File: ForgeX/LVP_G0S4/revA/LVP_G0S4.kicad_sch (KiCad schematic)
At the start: 73 parts, among them J1 Conn_02x05_Odd_Even, J10 Conn_01x02_Pin, J11 Conn_01x02_Pin, J12 Conn_01x02_Pin, J13 Conn_01x02_Pin, J14 Conn_02x05_Odd_Even, J16 Conn_01x04, J17 Conn_01x04, J2 Conn_02x05_Odd_Even, J3 Conn_02x05_Odd_Even, J4 Conn_02x05_Odd_Even, J5 Conn_01x04_Pin, J6 Conn_02x20_Odd_Even, J7 Conn_01x02_Pin, J8 Conn_01x02_Pin, J9 Screw_Terminal_01x09, Q2 AO3400A, U1 SP485EEN-TD, U2 SP485EEN-TD, U3 SP485EEN-TD, U4 AMS1117-3.3, U5 LM311, U6 LM311, U7 LM311

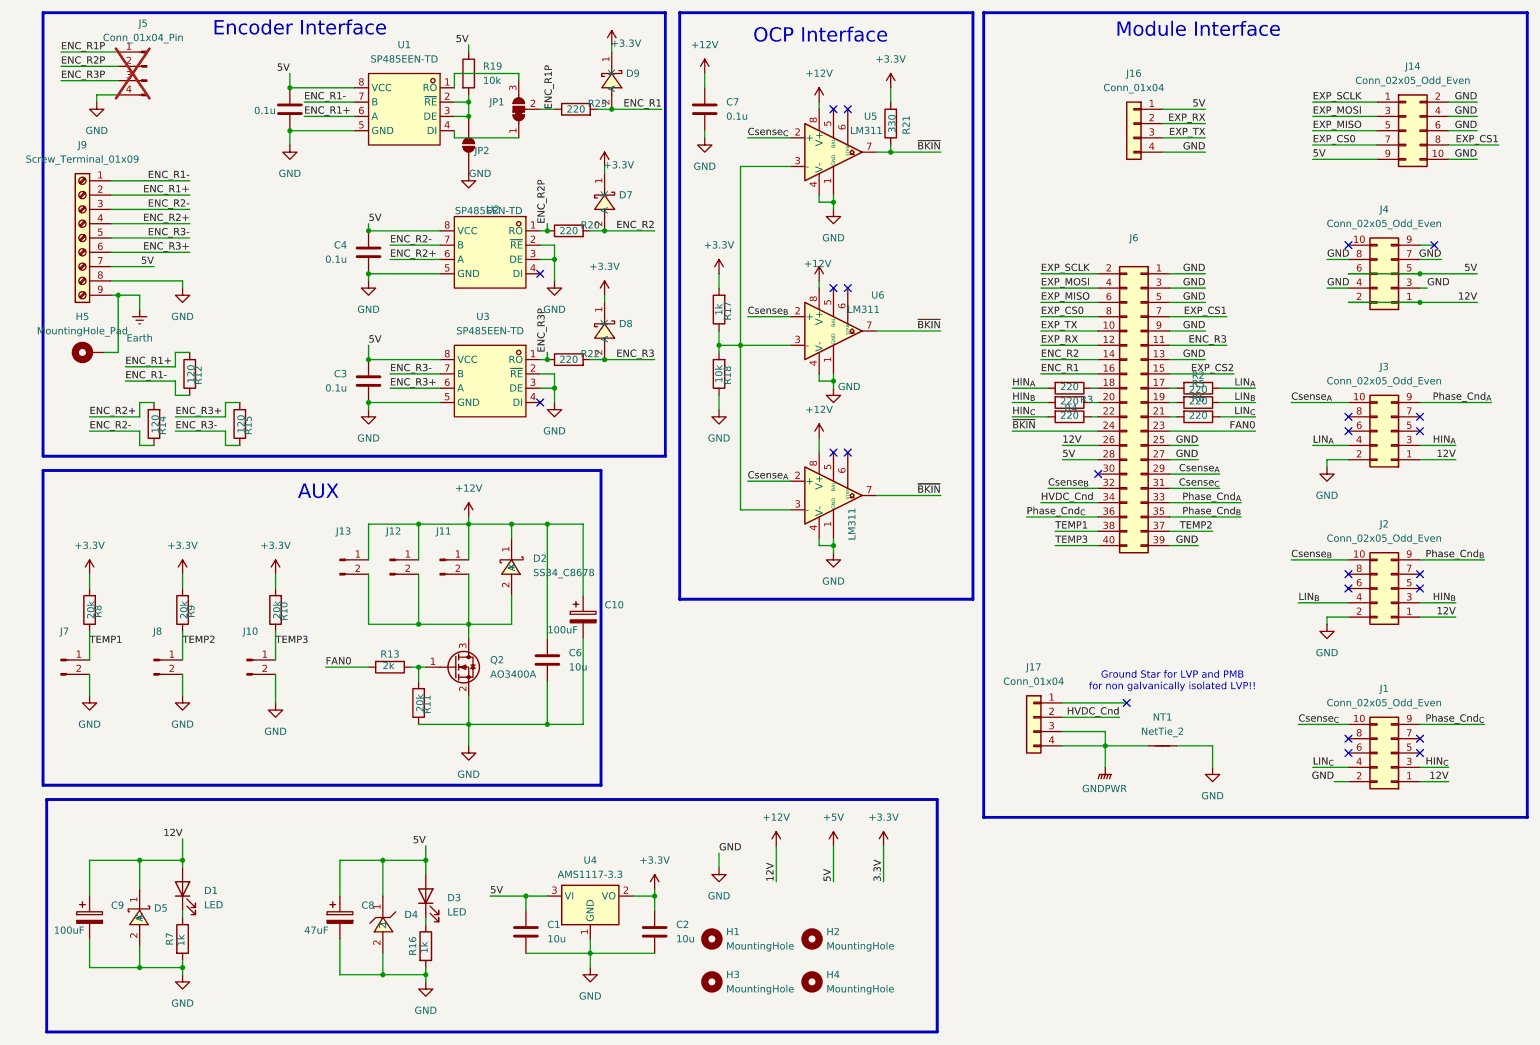
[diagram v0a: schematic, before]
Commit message: LVP OCP comparators removal
Initiallly put for short circuit protection, and quick analysis reveals they are not fit for the use case , and add complexity there , OCP can be included in HBM much better or in MGD's
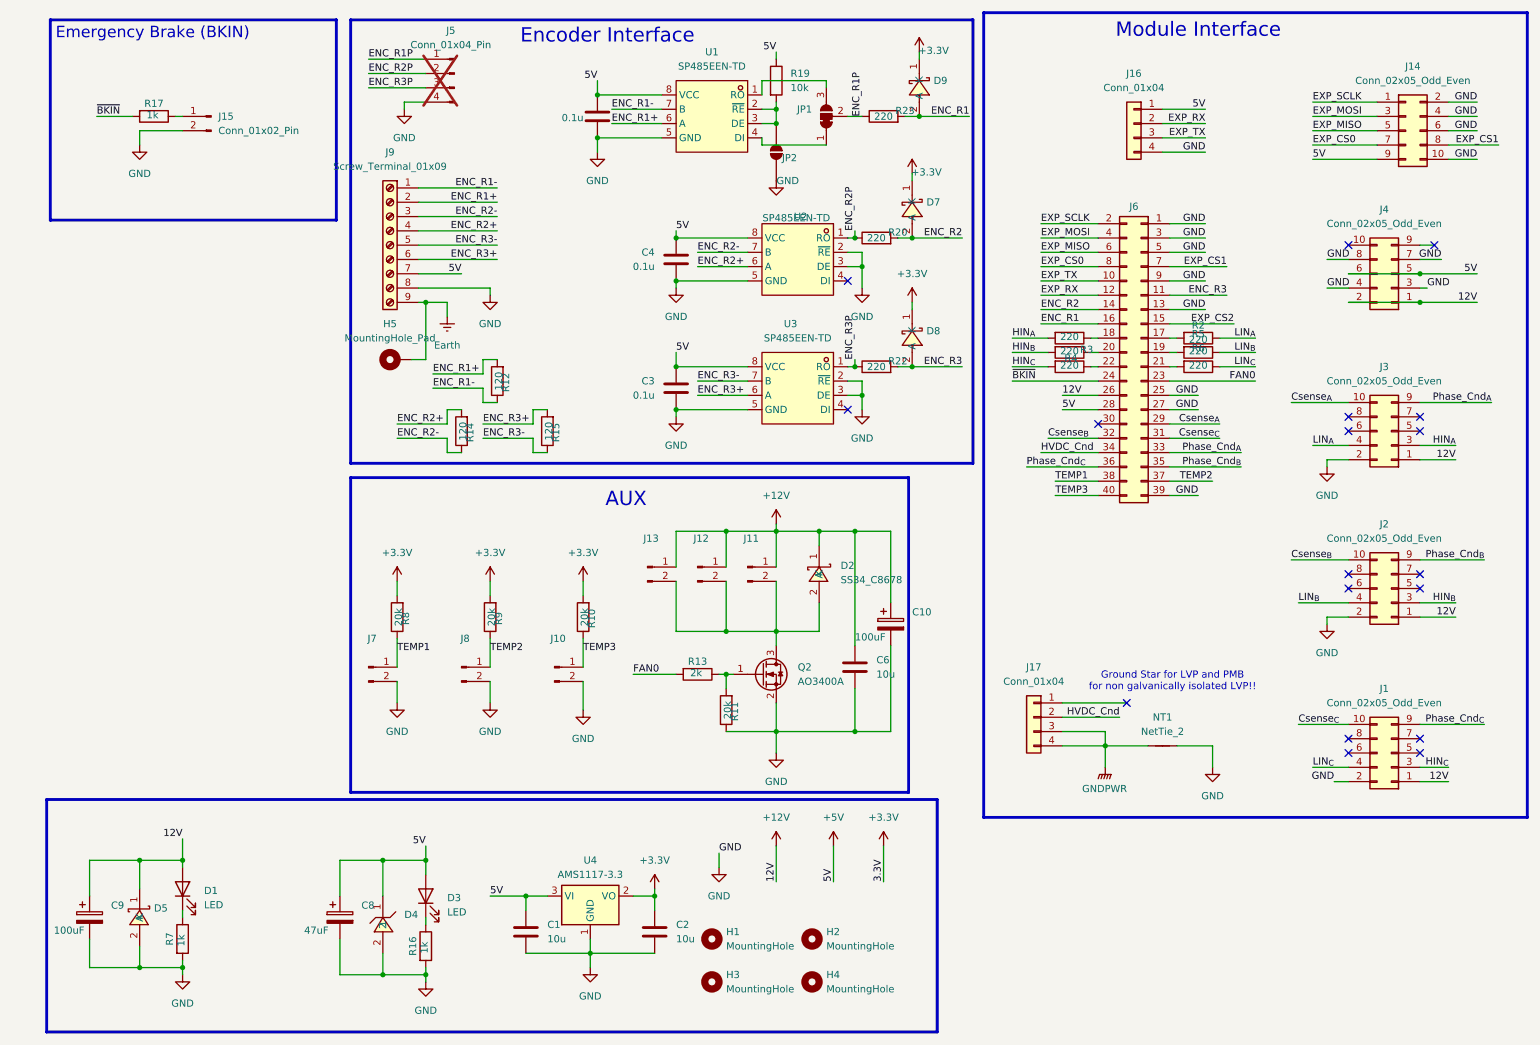
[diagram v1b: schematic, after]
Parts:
- removed C7: 0.1u, Capacitor_SMD:C_1206_3216Metric_Pad1.33x1.80mm_HandSolder, symbol Device:C
- removed R18: 10k, Resistor_SMD:R_0603_1608Metric_Pad0.98x0.95mm_HandSolder, symbol Device:R
- removed R21: 330, Resistor_SMD:R_0603_1608Metric_Pad0.98x0.95mm_HandSolder, symbol Device:R
- removed U5, U6, U7: LM311, Package_SO:SOIC-8_3.9x4.9mm_P1.27mm, symbol Comparator:LM311
- added J15: Conn_01x02_Pin, Connector_JST:JST_XH_B2B-XH-A_1x02_P2.50mm_Vertical, symbol Connector:Conn_01x02_Pin
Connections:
- net +3.3V: no longer R17.2
- net GND: now also J15.2 (Pin_2)
- net ~{BKIN}: now also R17.2
- net at R17.1: now also J15.1 (Pin_1)
- no-connect marks 24 -> 18
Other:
- note removed: "OCP Interface"
- moved on the sheet: C10, C3, C4, C6, D2, D7, D8, D9, H5, J10, J11, J12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
